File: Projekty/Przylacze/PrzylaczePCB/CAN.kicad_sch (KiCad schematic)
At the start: 49 parts, among them SW1 SW_SPDT, SW2 SW_SPDT, SW3 SW_SPDT, SW4 SW_SPDT, SW5 SW_SPDT, SW6 SW_SPDT, SW7 SW_SPDT, SW8 SW_SPDT, U1 MCP2515-xSO, U2 TJA1055T_3_C,518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

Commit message: Przyłącze - schemat elektryczny v1.2
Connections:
- no-connect marks 0 -> 3
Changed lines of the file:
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@@
   (junction (at 213.36 128.27) (diameter 0) (color 0 0 0 0)
   )
+  (no_connect (at 218.44 33.02))
+  (no_connect (at 218.44 53.34))
+  (no_connect (at 58.42 120.65))
   (wire (pts (xy 181.61 38.1) (xy 205.74 38.1))
     (stroke (width 0) (type default))
@@
     (stroke (width 0) (type default))
   )
-  (wire (pts (xy 156.21 38.1) (xy 156.21 50.8))
-    (stroke (width 0) (type default))
-  )
   (wire (pts (xy 45.72 115.57) (xy 58.42 115.57))
     (stroke (width 0) (type default))
@@
     (stroke (width 0) (type default))
   )
+  (wire (pts (xy 26.67 85.09) (xy 26.67 88.9))
+    (stroke (width 0) (type default))
+  )
   (wire (pts (xy 152.4 43.18) (xy 161.29 43.18))
     (stroke (width 0) (type default))
@@
     (stroke (width 0) (type default))
   )
-  (wire (pts (xy 26.67 85.09) (xy 26.67 88.9))
-    (stroke (width 0) (type default))
-  )
   (wire (pts (xy 119.38 52.07) (xy 120.65 52.07))
     (stroke (width 0) (type default))
@@
     (stroke (width 0) (type default))
   )
-  (wire (pts (xy 161.29 43.18) (xy 161.29 50.8))
-    (stroke (width 0) (type default))
-  )
   (wire (pts (xy 54.61 135.89) (xy 58.42 135.89))
     (stroke (width 0) (type default))
@@
     (stroke (width 0) (type default))
   )
+  (wire (pts (xy 156.21 38.1) (xy 156.21 55.88))
+    (stroke (width 0) (type default))
+  )
   (wire (pts (xy 213.36 140.97) (xy 210.82 140.97))
     (stroke (width 0) (type default))
@@
   )
   (wire (pts (xy 250.19 53.34) (xy 250.19 33.02))
+    (stroke (width 0) (type default))
+  )
+  (wire (pts (xy 161.29 43.18) (xy 161.29 55.88))
     (stroke (width 0) (type default))
   )
@@
     )
   )
-  (global_label "RXD_HS" (shape input) (at 21.59 46.99 180) (fields_autoplaced)
+  (global_label "RXD_HS" (shape output) (at 21.59 46.99 180) (fields_autoplaced)
     (effects (font (size 1 1)) (justify right))
     (property "Intersheetrefs" "${INTERSHEET_REFS}" (at 13.5878 46.99 0)
@@
     )
   )
-  (global_label "TXD_HS" (shape output) (at 21.59 44.45 180) (fields_autoplaced)
+  (global_label "TXD_HS" (shape input) (at 21.59 44.45 180) (fields_autoplaced)
     (effects (font (size 1 1)) (justify right))
     (property "Intersheetrefs" "${INTERSHEET_REFS}" (at 13.8259 44.45 0)
@@
     )
   )
-  (global_label "TXD_FT" (shape output) (at 53.34 128.27 180) (fields_autoplaced)
+  (global_label "TXD_FT" (shape input) (at 53.34 128.27 180) (fields_autoplaced)
     (effects (font (size 1 1)) (justify right))
     (property "Intersheetrefs" "${INTERSHEET_REFS}" (at 45.9569 128.27 0)
@@
     )
   )
-  (global_label "RXD_FT" (shape input) (at 53.34 140.97 180) (fields_autoplaced)
+  (global_label "RXD_FT" (shape output) (at 53.34 140.97 180) (fields_autoplaced)
     (effects (font (size 1 1)) (justify right))
     (property "Intersheetrefs" "${INTERSHEET_REFS}" (at 45.7188 140.97 0)
@@
     )
   )
-  (symbol (lib_id "Device:R") (at 64.77 54.61 0) (unit 1)
-    (in_bom yes) (on_board yes) (dnp no) (fields_autoplaced)
-    (property "Reference" "R7" (at 67.31 53.975 0)
+  (symbol (lib_id "Device:R") (at 64.77 54.61 0) (mirror y) (unit 1)
+    (in_bom yes) (on_board yes) (dnp no)
+    (property "Reference" "R7" (at 62.23 53.975 0)
       (effects (font (size 1.27 1.27)) (justify left))
     )
-    (property "Value" "62" (at 67.31 56.515 0)
+    (property "Value" "62" (at 62.23 56.515 0)
       (effects (font (size 1.27 1.27)) (justify left))
     )
-    (property "Footprint" "Resistor_THT:R_Axial_DIN0207_L6.3mm_D2.5mm_P10.16mm_Horizontal" (at 62.992 54.61 90)
+    (property "Footprint" "Resistor_THT:R_Axial_DIN0207_L6.3mm_D2.5mm_P10.16mm_Horizontal" (at 66.548 54.61 90)
       (effects (font (size 1.27 1.27)) hide)
     )
@@
   )
   (symbol (lib_id "Diode:BZV55B56") (at 181.61 48.26 270) (unit 1)
-    (in_bom yes) (on_board yes) (dnp no) (fields_autoplaced)
-    (property "Reference" "D6" (at 184.15 47.625 90)
+    (in_bom yes) (on_board yes) (dnp no)
+    (property "Reference" "D6" (at 170.18 48.26 90)
       (effects (font (size 1.27 1.27)) (justify left))
     )
-    (property "Value" "Zener 10V" (at 184.15 50.165 90)
+    (property "Value" "Zener 10V" (at 170.18 50.8 90)
       (effects (font (size 1.27 1.27)) (justify left))
     )

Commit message: Przyłącze - projekt PCB v0.2
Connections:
- net at C7.2, U1.7 (OSC2): now also Y1.1; no longer Y1.2
- net at C8.2, U1.8 (OSC1): now also Y1.2; no longer Y1.1
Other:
- moved on the sheet: Y1

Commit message: Przyłącze - projekt PCB v1.1
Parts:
- D3, D4, D5: footprint 1_WLASNA_Library:2PAD_WIRE -> Connector_PinHeader_2.54mm:PinHeader_1x02_P2.54mm_Vertical
- H1: footprint 1_WLASNA_Library:4Pin_COMMON_MODE_CHOKE_B82787C0104H002 -> PrzylaczeFootprintLibrary:4Pin_COMMON_MODE_CHOKE_B82787C0104H002
- SW1, SW2, SW3, SW4, SW5, SW6, SW7, SW8: footprint 1_WLASNA_Library:3PAD_WIRE_SWITCH -> Connector_PinHeader_2.54mm:PinHeader_1x03_P2.54mm_Vertical

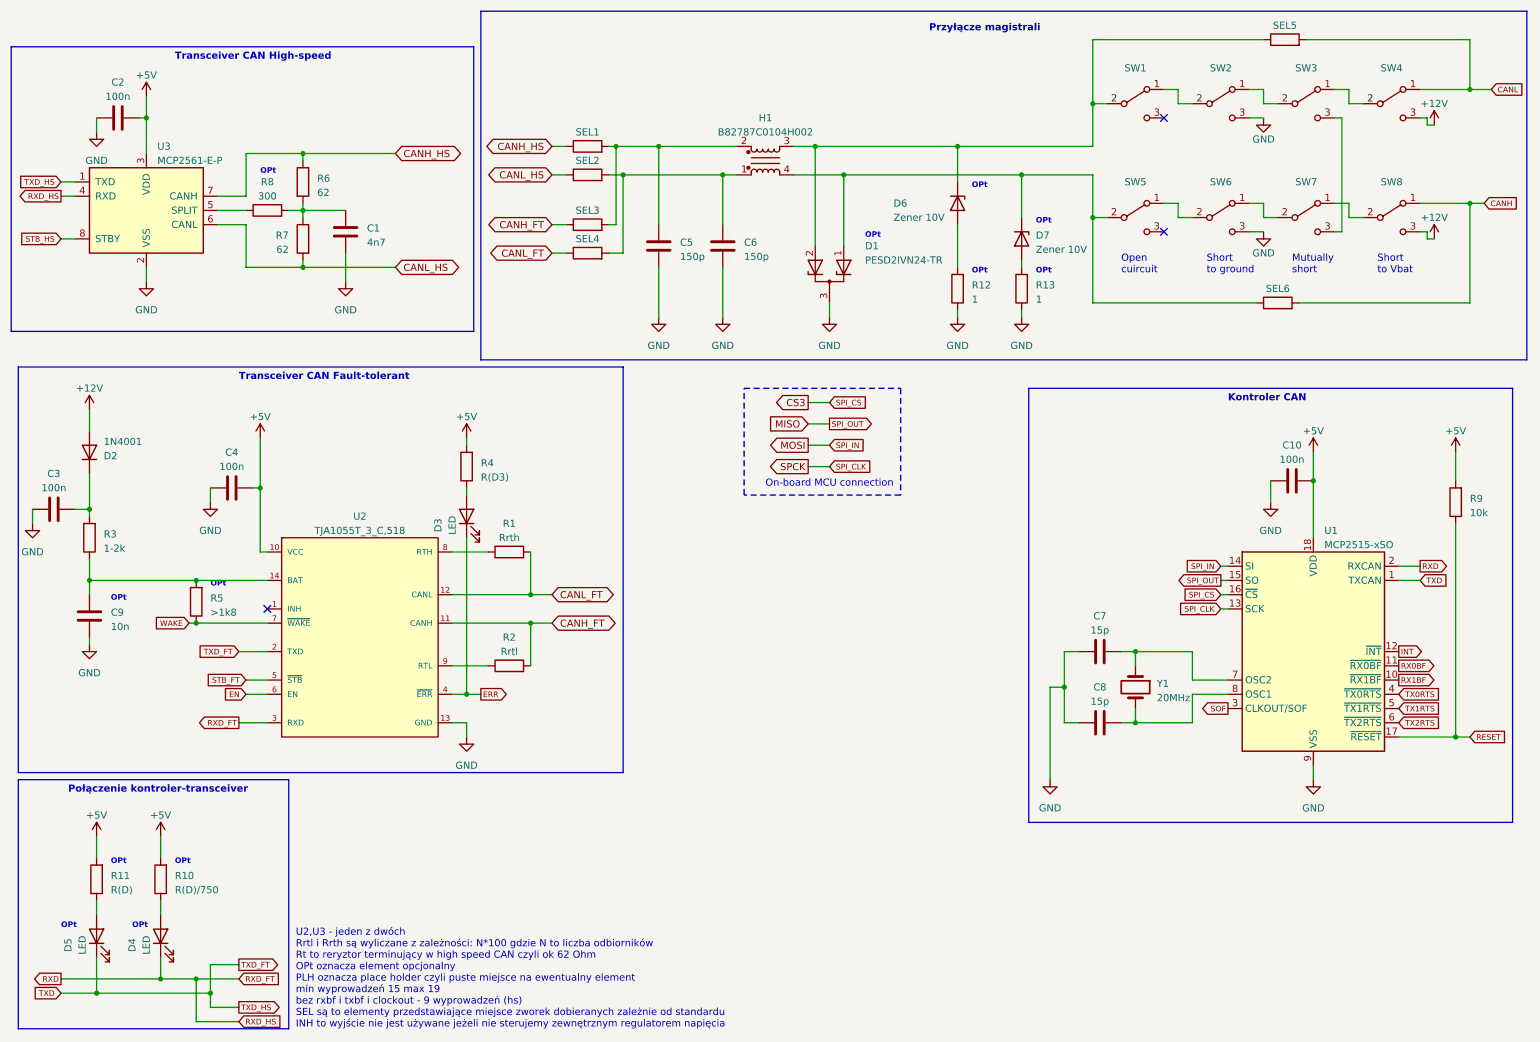
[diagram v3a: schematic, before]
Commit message: Przyłącze - projekt PCB v1.5
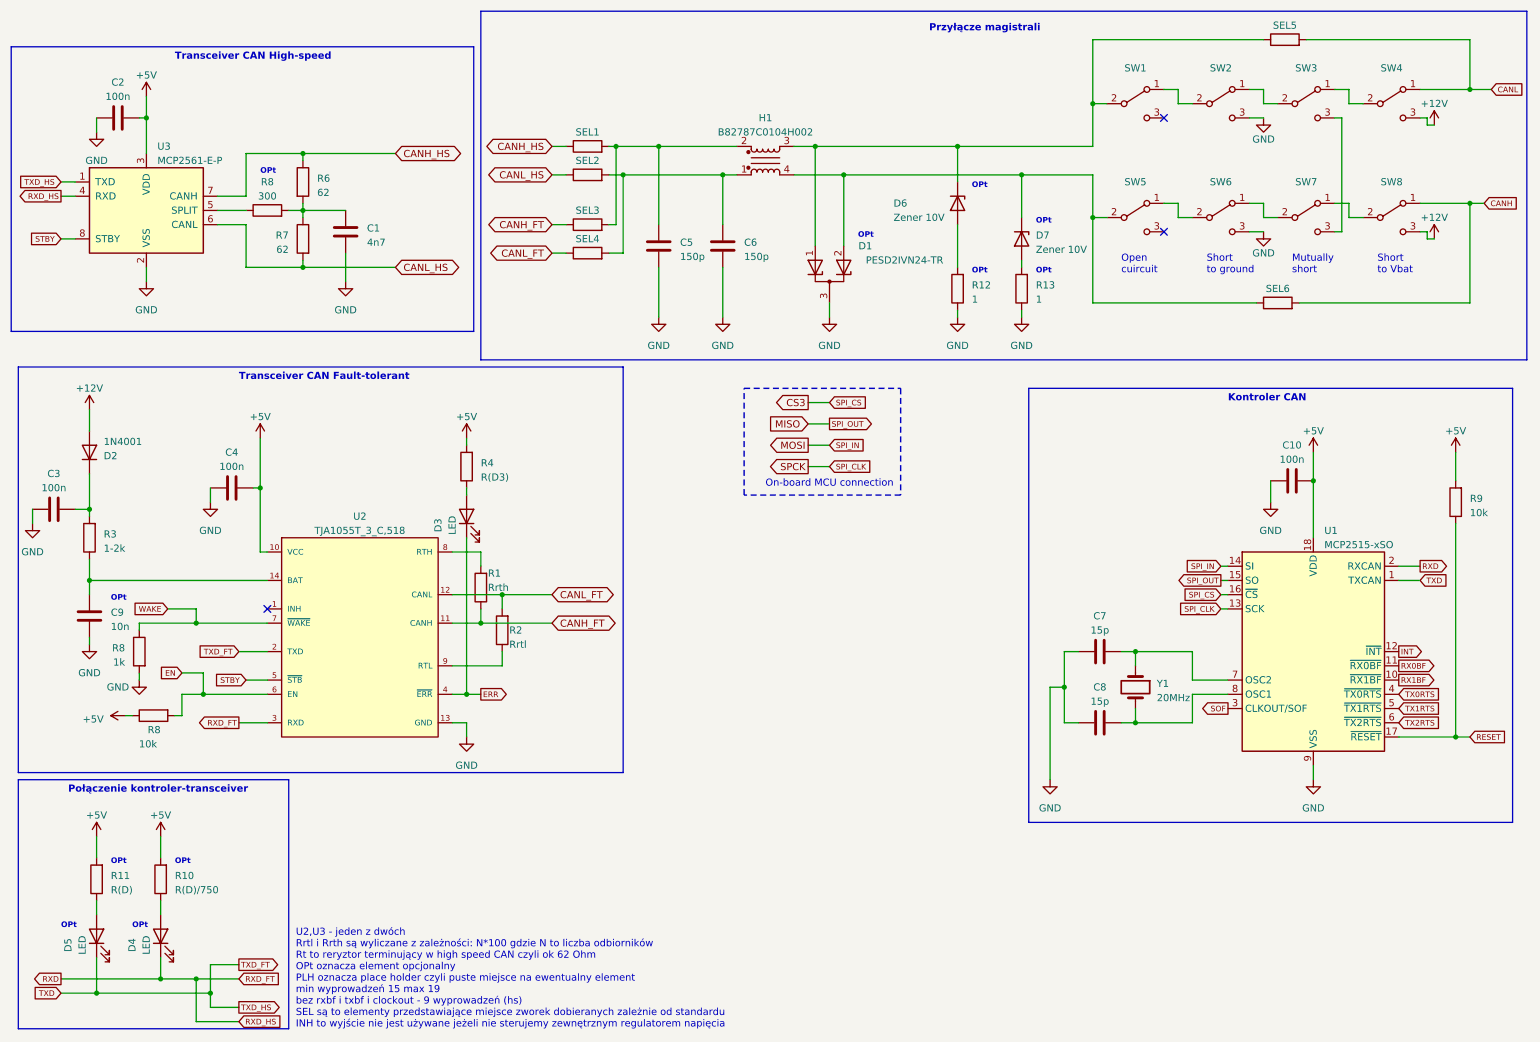
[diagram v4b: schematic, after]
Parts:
- removed R5: >1k8, Resistor_THT:R_Axial_DIN0207_L6.3mm_D2.5mm_P10.16mm_Horizontal, symbol Device:R
- added R8: 10k, Resistor_THT:R_Axial_DIN0207_L6.3mm_D2.5mm_P10.16mm_Horizontal, symbol Device:R
- added R8: 1k, Resistor_THT:R_Axial_DIN0207_L6.3mm_D2.5mm_P10.16mm_Horizontal, symbol Device:R
- SEL1, SEL2, SEL3, SEL4, SEL5, SEL6: footprint Resistor_SMD:R_0805_2012Metric -> Jumper:SolderJumper-2_P1.3mm_Open_RoundedPad1.0x1.5mm
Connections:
- net STB_HS is gone; now on net STBY: U3.8 (STBY)
- net +5V: now also R8.1
- net CANH_FT: now also R1.1; no longer R2.2
- net CANL_FT: now also R2.2; no longer R1.2
- net EN: now also R8.2
- net GND: now also R8.2
- net WAKE: now also R8.1
- net at D7.1 (K), H1.4, SEL6.1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: now also D1.2 (K); no longer D1.1 (K)
- net at U2.8 (RTH): now also R1.2; no longer R1.1
- net at D6.1 (K), H1.3, SEL5.1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: now also D1.1 (K); no longer D1.2 (K)
- net STB_FT renamed STBY
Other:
- moved on the sheet: D1, R1, R2

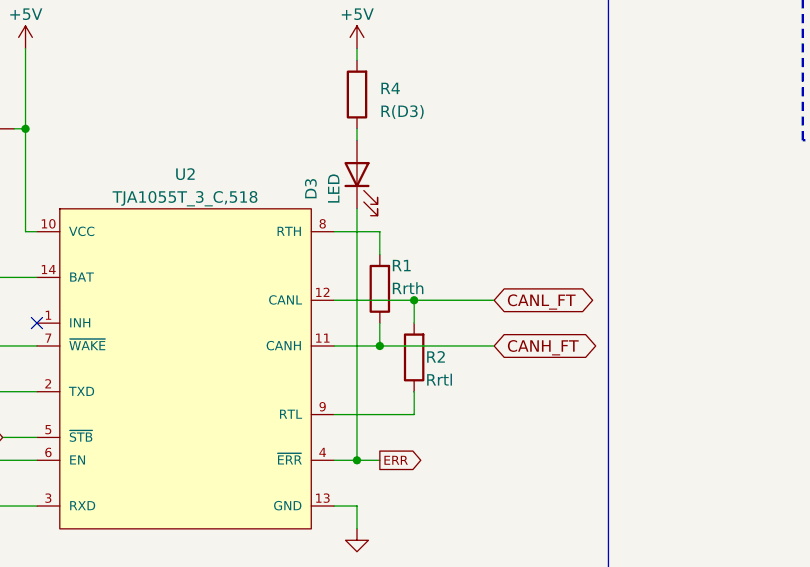
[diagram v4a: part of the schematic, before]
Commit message: Przyłącze - projekt PCB v1.5.1
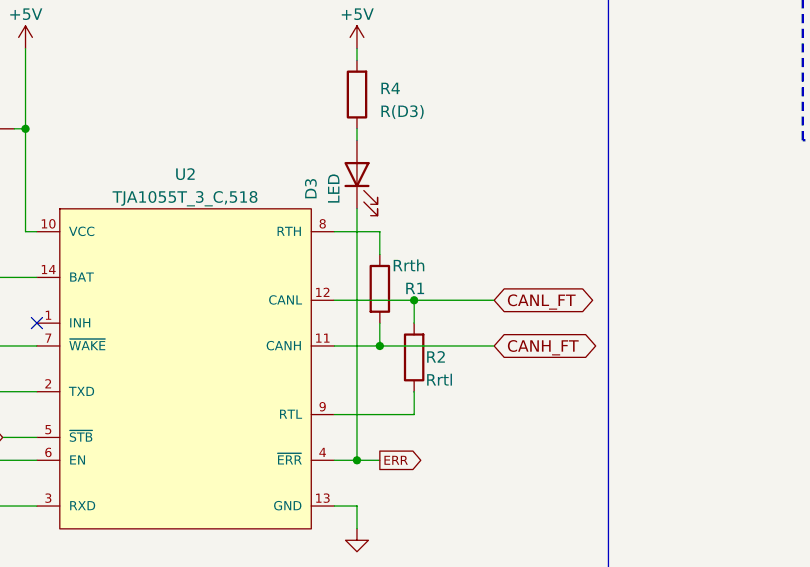
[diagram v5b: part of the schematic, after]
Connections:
- net CANH_FT: now also R1.2; no longer R1.1
- net at U2.8 (RTH): now also R1.1; no longer R1.2
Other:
- moved on the sheet: R1
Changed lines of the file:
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@@
     )
   )
-  (symbol (lib_id "Device:R") (at 96.52 116.84 180) (unit 1)
+  (symbol (lib_id "Device:R") (at 96.52 116.84 0) (unit 1)
     (in_bom yes) (on_board yes) (dnp no)
-    (property "Reference" "R1" (at 97.79 114.3 0)
+    (property "Reference" "R1" (at 101.6 116.84 0)
       (effects (font (size 1.27 1.27)) (justify right))
     )
-    (property "Value" "Rrth" (at 97.79 116.84 0)
+    (property "Value" "Rrth" (at 101.6 114.3 0)
       (effects (font (size 1.27 1.27)) (justify right))
     )
-    (property "Footprint" "Resistor_THT:R_Axial_DIN0207_L6.3mm_D2.5mm_P10.16mm_Horizontal" (at 98.298 116.84 90)
+    (property "Footprint" "Resistor_THT:R_Axial_DIN0207_L6.3mm_D2.5mm_P10.16mm_Horizontal" (at 94.742 116.84 90)
       (effects (font (size 1.27 1.27)) hide)
     )

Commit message: Przyłącze - projekt PCB v1.5.2
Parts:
- Y1: footprint Crystal:Crystal_SMD_HC49-SD_HandSoldering -> Crystal:Crystal_SMD_HC49-SD
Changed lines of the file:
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@@
       (effects (font (size 1.27 1.27)) (justify left))
     )
-    (property "Footprint" "Crystal:Crystal_SMD_HC49-SD_HandSoldering" (at 213.36 134.62 0)
+    (property "Footprint" "Crystal:Crystal_SMD_HC49-SD" (at 213.36 134.62 0)
       (effects (font (size 1.27 1.27)) hide)
     )
